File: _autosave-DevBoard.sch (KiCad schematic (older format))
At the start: 29 parts, among them J1 Conn_01x06, J2 USB_B_Micro, J3 Debug Headers, J4 MIDI_TX_Out, SW1 SW_Push, U1 STM32L476RCTx, U2 LD1117S33CTR

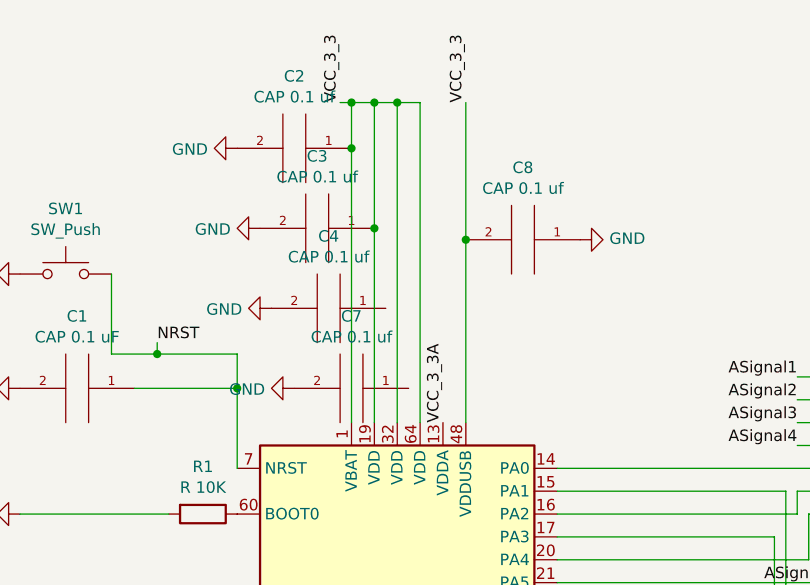
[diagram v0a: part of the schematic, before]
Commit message: added board layout
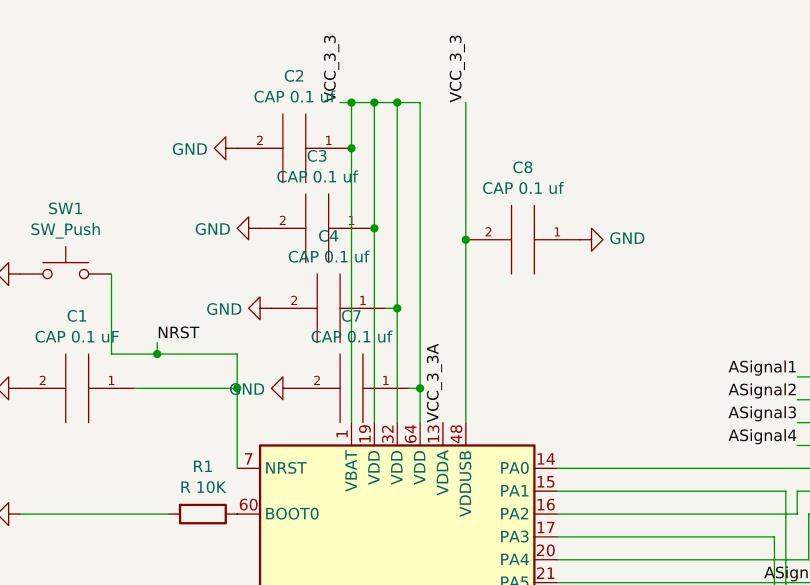
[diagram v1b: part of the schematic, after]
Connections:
- net G_3.3: now also C4.1, C7.1
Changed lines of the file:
@@
 	2200 850  2200 1400
 Wire Wire Line
-	2400 850  2400 2250
+	2400 850  2400 2100
 $Comp
 L pspice:CAP C2
@@
 $EndComp
 Wire Wire Line
-	2300 850  2300 2250
+	2300 850  2300 1750
 $Comp
 L pspice:CAP C7
@@
 $EndComp
 $Comp
-L power:GND #PWR?
+L power:GND #PWR0101
 U 1 1 5FC5D45C
 P 5550 1250
-F 0 "#PWR?" H 5550 1000 50  0001 C CNN
+F 0 "#PWR0101" H 5550 1000 50  0001 C CNN
 F 1 "GND" V 5555 1122 50  0000 R CNN
 F 2 "" H 5550 1250 50  0001 C CNN
@@
 	0    1    1    0
 $EndComp
+Wire Wire Line
+	2350 2100 2400 2100
+Connection ~ 2400 2100
+Wire Wire Line
+	2400 2100 2400 2250
+Wire Wire Line
+	2250 1750 2300 1750
+Connection ~ 2300 1750
+Wire Wire Line
+	2300 1750 2300 2250
 $EndSCHEMATC
